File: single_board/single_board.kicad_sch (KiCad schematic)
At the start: 120 parts, among them J1 SWD, J11 SPI Debug, J17 BOOTSEL, J2 USB_C_Receptacle_USB2.0_16P, J3 RST, J30 JST_GH_H, J31 JST_GH_H, J32 PB_Vertical, J33 JST_GH_H, J34 PB_Vertical, J35 JST_GH_H, J36 JST_GH_H, J37 JST_GH_H, J38 PB_Vertical, J39 PB_Vertical, J4 Conn_01x02, J40 PB_Vertical, J41 PB_Vertical, J42 PB_Vertical, J43 PB_Vertical, J44 PB_Vertical, J45 PB_Vertical, J46 PB_Vertical, J47 PB_Vertical, J48 PB_Vertical, J49 PB_Vertical, J5 Conn_01x02, J50 PB_Vertical, J6 Conn_01x02, J7 Conn_01x02, Q1 AO3401A, Q2 AO3401A, Q3 AO3401A, Q4 AO3401A, Q5 2N7002, SW1 Button, U1 AP2112K-3.3, U3 USBLC6-2SC6, U4 LSM6DSV, U5 STM32G474VBTx, Y1 FC-135

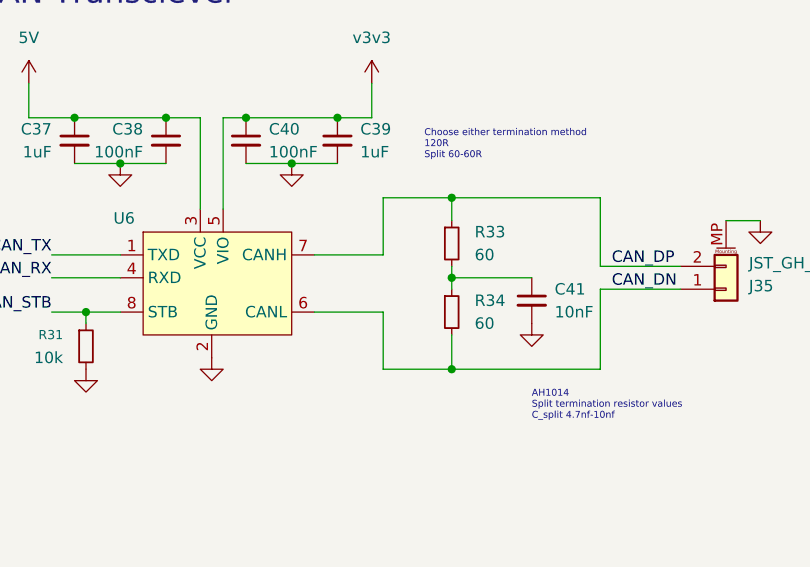
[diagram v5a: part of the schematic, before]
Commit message: Controls Board Version 0
Rough layout of Elec Controls Board. SIlkscreen in progress. New schematic changes have not been incorporated fully yet. SIzed 100 x 95 mm
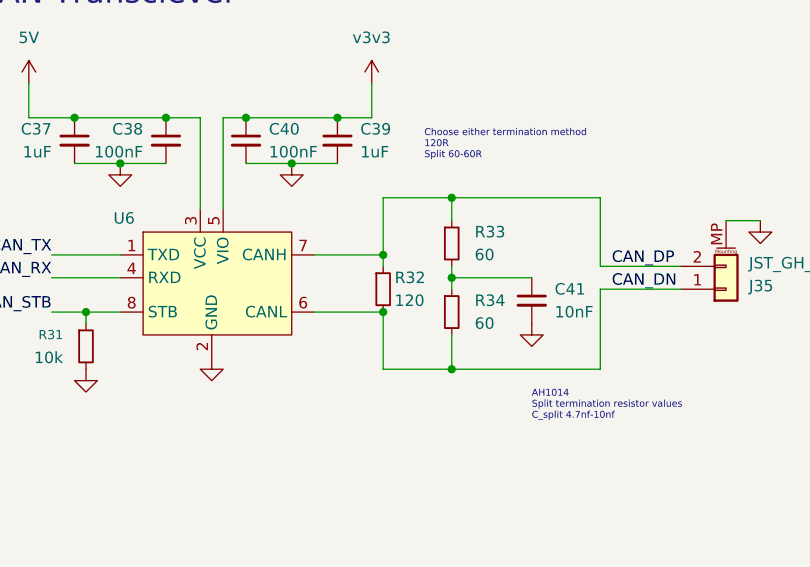
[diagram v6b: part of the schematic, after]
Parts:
- added R32: 120, Resistor_SMD:R_0402_1005Metric, symbol Device:R_Small
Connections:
- net CAN_DN: now also R32.2
- net CAN_DP: now also R32.1
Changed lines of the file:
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@@
 	)
 	(junction
+		(at 261.62 53.34)
+		(diameter 0)
+		(color 0 0 0 0)
+	)
+	(junction
 		(at 38.1 257.81)
 		(diameter 0)
@@
 	)
 	(junction
+		(at 261.62 46.99)
+		(diameter 0)
+		(color 0 0 0 0)
+	)
+	(junction
 		(at 41.91 243.84)
 		(diameter 0)
@@
 	(wire
 		(pts
+			(xy 261.62 46.99) (xy 261.62 48.26)
+		)
+		(stroke
+			(width 0)
+			(type default)
+		)
+	)
+	(wire
+		(pts
 			(xy 294.64 109.22) (xy 297.18 109.22)
 		)
@@
 					(unit 1)
 				)
+			)
+		)
+	)
+	(symbol
+		(lib_id "Device:R_Small")
+		(at 261.62 50.8 0)
+		(unit 1)
+		(body_style 1)
+		(exclude_from_sim no)
+		(in_bom yes)
+		(on_board yes)
+		(in_pos_files yes)
+		(dnp no)
+		(property "Reference" "R32"
+			(at 262.89 49.5299 0)
+			(show_name no)
+			(do_not_autoplace no)
+			(effects
+				(font
+					(size 1.27 1.27)
+				)
+				(justify left)
+			)
+		)
+		(property "Value" "120"
+			(at 262.89 52.0699 0)
+			(show_name no)
+			(do_not_autoplace no)
+			(effects
+				(font
+					(size 1.27 1.27)
+				)
+				(justify left)
+			)
+		)
+		(property "Footprint" "Resistor_SMD:R_0402_1005Metric"
+			(at 261.62 50.8 0)
+			(hide yes)
+			(show_name no)
+			(do_not_autoplace no)
+			(effects
+				(font
+					(size 1.27 1.27)
+				)
+			)
+		)
+		(property "Datasheet" ""
+			(at 261.62 50.8 0)
+			(hide yes)
+			(show_name no)
+			(do_not_autoplace no)
+			(effects
+				(font
+					(size 1.27 1.27)
+				)
+			)
+		)
+		(property "Description" "Resistor, small symbol"
+			(at 261.62 50.8 0)
+			(hide yes)
+			(show_name no)
+			(do_not_autoplace no)
+			(effects
+				(font
+					(size 1.27 1.27)
+				)
+			)
+		)
+		(pin "1"
+		)
+		(pin "2"
+		)
+		(instances
+			(project "single_board"
+				(path "/ae10586e-ebf8-402d-a979-c2f011cdeee2"
+					(reference "R32")
+					(unit 1)
+				)

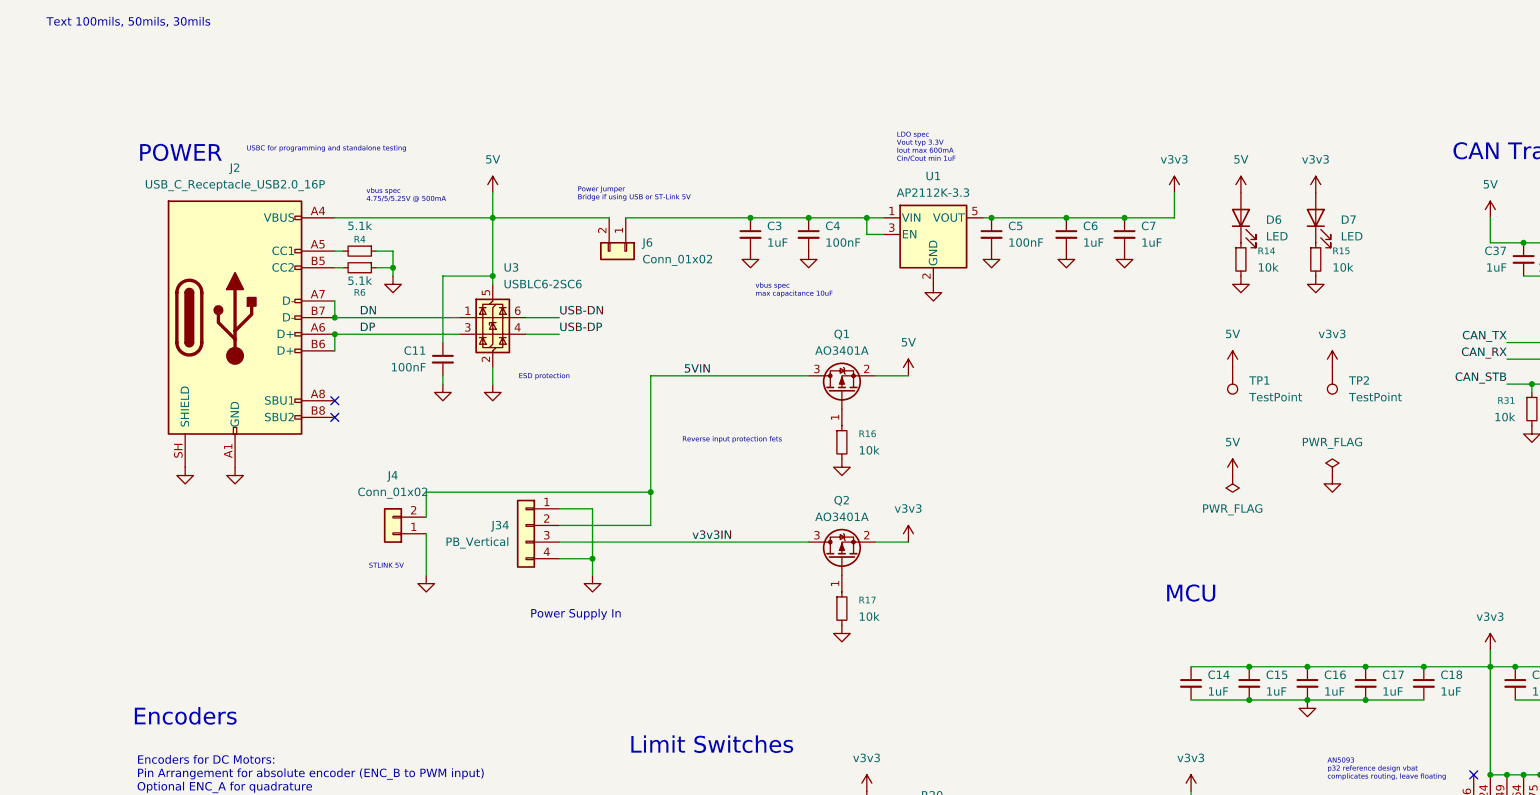
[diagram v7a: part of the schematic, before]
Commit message: Updated schematic (power)
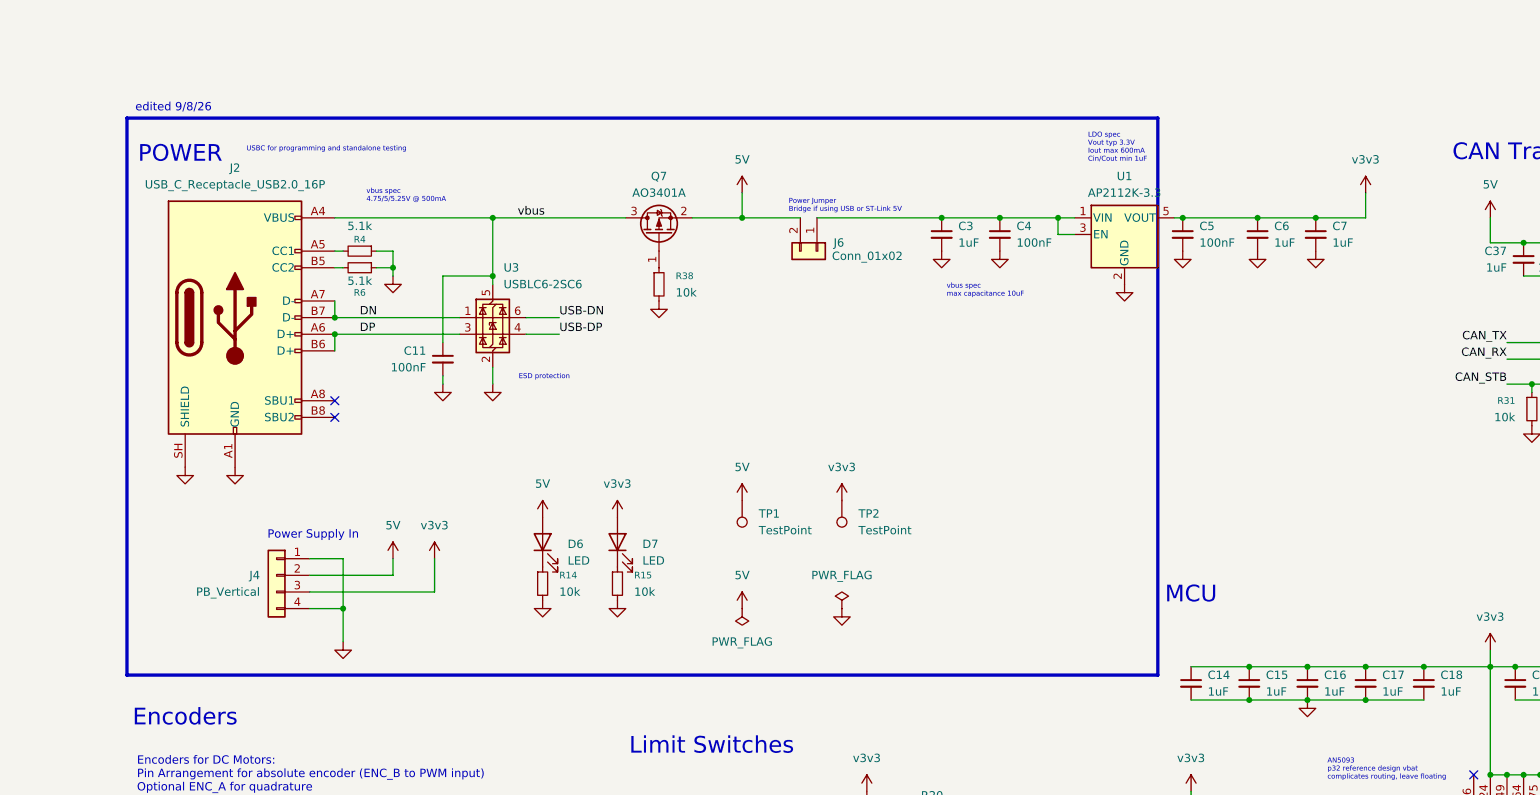
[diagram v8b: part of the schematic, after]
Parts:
- removed J34: PB_Vertical, Connector_Molex:Molex_PicoBlade_53047-0410_1x04_P1.25mm_Vertical, symbol Connector_Generic:Conn_01x04
- removed J4: Conn_01x02, Connector_PinHeader_2.54mm:PinHeader_1x02_P2.54mm_Vertical, symbol Connector_Generic:Conn_01x02
- removed Q1, Q2: AO3401A, Package_TO_SOT_SMD:SOT-23, symbol Transistor_FET:AO3401A
- removed R16, R17: 10k, Resistor_SMD:R_0402_1005Metric, symbol Device:R_Small
- added J4: PB_Vertical, Connector_Molex:Molex_PicoBlade_53047-0410_1x04_P1.25mm_Vertical, symbol Connector_Generic:Conn_01x04
- added Q7: AO3401A, Package_TO_SOT_SMD:SOT-23, symbol Transistor_FET:AO3401A
- added R38: 10k, Resistor_SMD:R_0402_1005Metric, symbol Device:R_Small
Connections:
- net 5V: now also J4.2 (Pin_2), Q7.2 (S); no longer C11.1, J2.A4 (VBUS), J2.A9 (VBUS), J2.B4 (VBUS), J2.B9 (VBUS), U3.5 (VBUS)
- net GND: now also J4.1 (Pin_1), J4.4 (Pin_4), R38.2
- net v3v3: now also J4.3 (Pin_3)
- new net: Q7.1 (G), R38.1
- new net vbus: C11.1, J2.A4 (VBUS), J2.A9 (VBUS), J2.B4 (VBUS), J2.B9 (VBUS), Q7.3 (D), U3.5 (VBUS)
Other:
- note added: "edited 9/8/26"
- note removed: "Reverse input protection fets"
- note removed: "STLINK 5V"
- note removed: "Text 100mils, 50mils, 30mils"
- moved on the sheet: C3, C4, C5, C6, C7, D6, D7, J6, R14, R15, TP1, TP2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
